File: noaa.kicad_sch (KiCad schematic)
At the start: 12 parts, among them J1 USB_C_Receptacle_USB2.0_16P, J2 SMA_F, J3 SMA_F, U1 MAX2659ELTT, U2 AMS1117-3.3

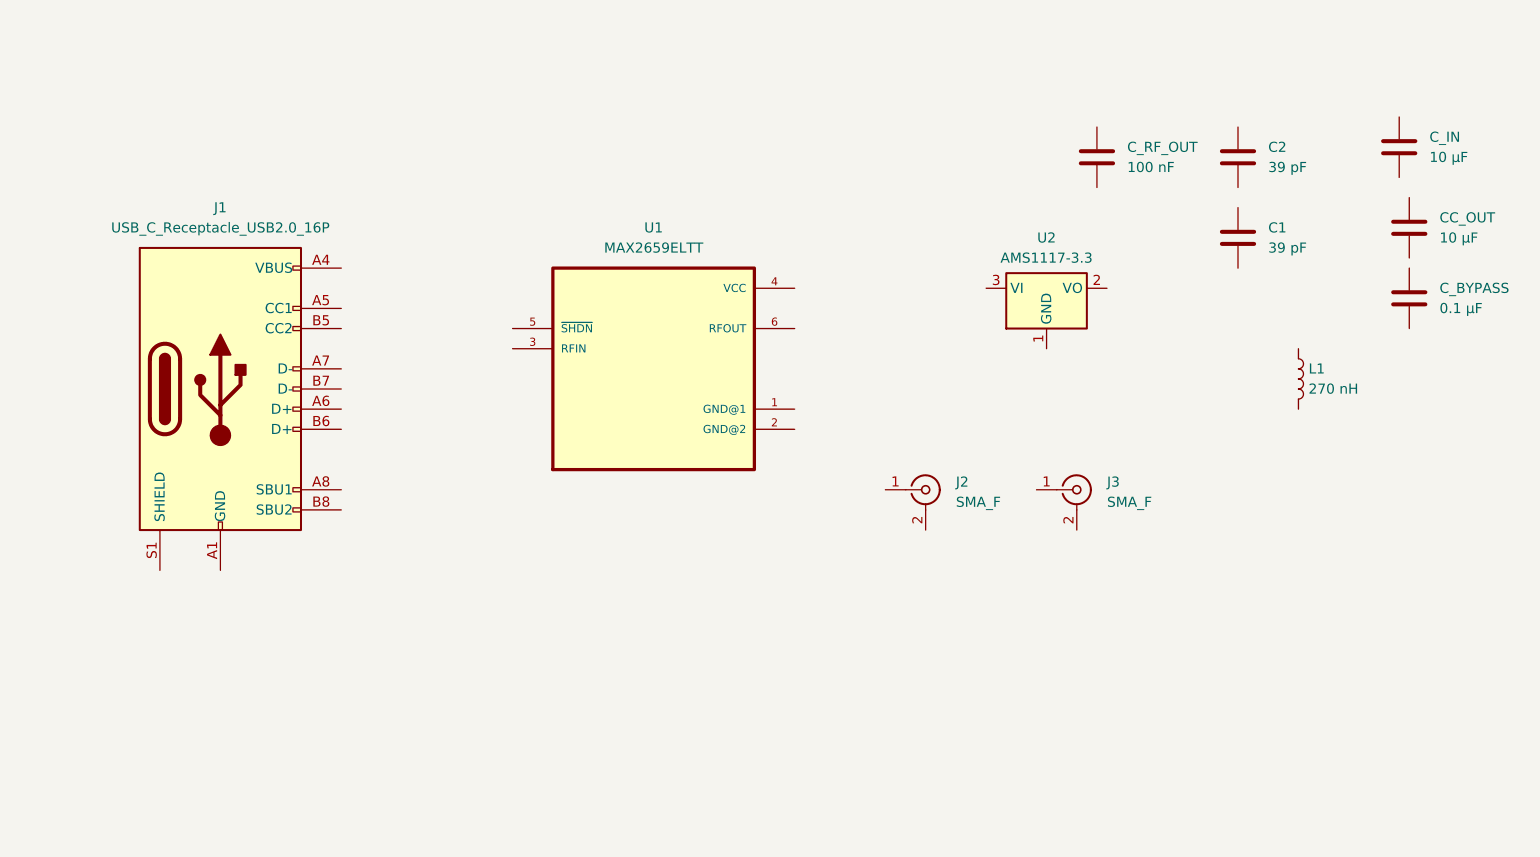
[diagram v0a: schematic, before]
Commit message: Added most of the schematic wiring. Still need to do some USB ground and ESD protections
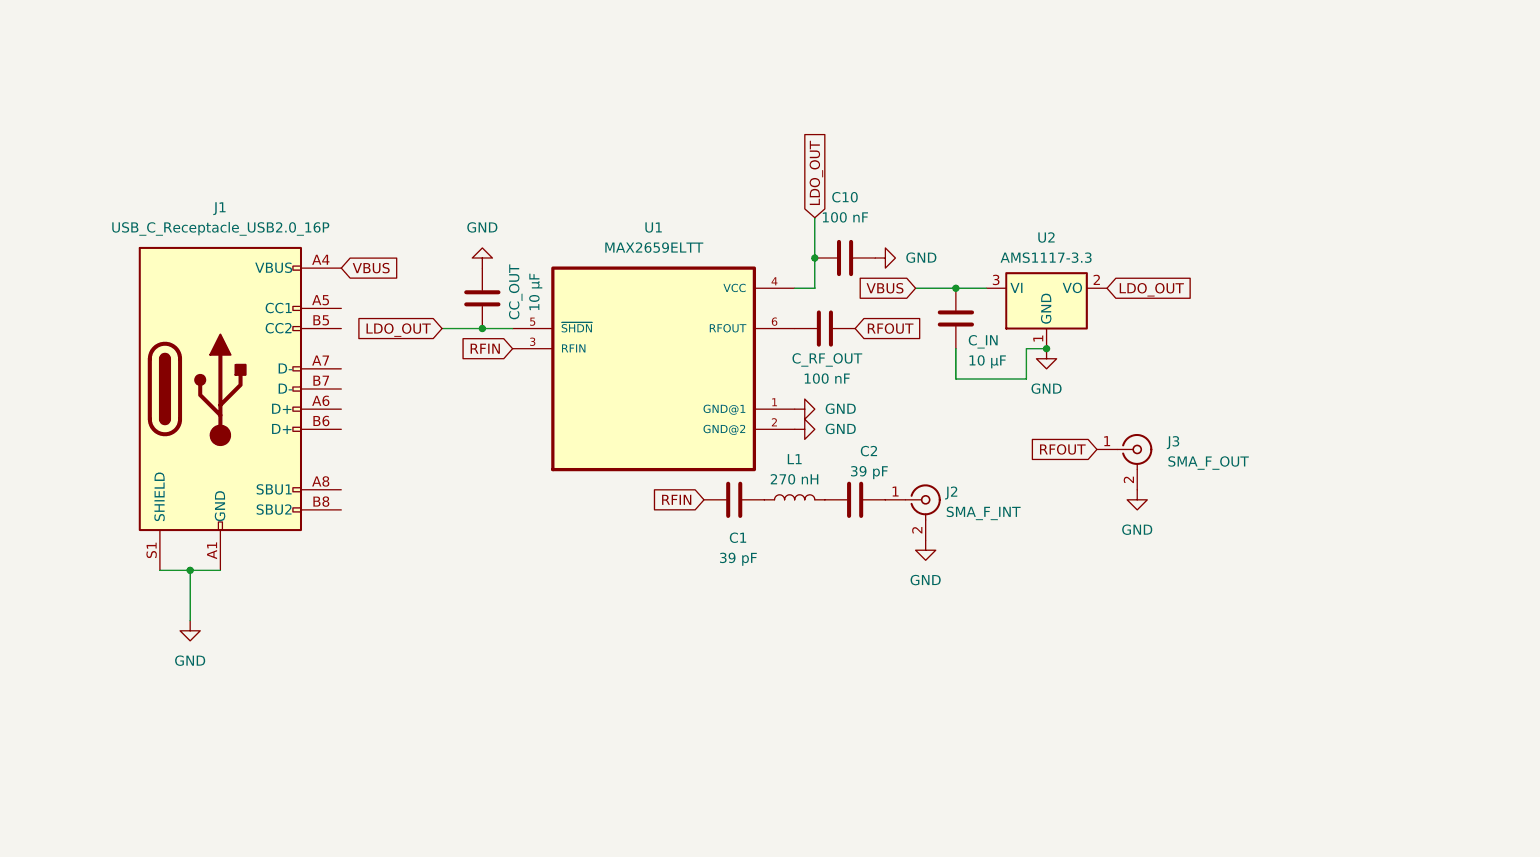
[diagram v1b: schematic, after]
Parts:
- removed C_BYPASS: 0.1 µF, symbol Device:C
- added C10: 100 nF, symbol Device:C
- J2: value SMA_F -> SMA_F_INT
- J3: value SMA_F -> SMA_F_OUT
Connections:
- net at C_RF_OUT.1: now also U1.6 (RFOUT)
- net RFOUT: now reaches C_RF_OUT.2
- net RFOUT: now also J3.1 (In)
- net at J2.1 (In): now also C2.2
- net GND: now reaches J2.2 (Ext)
- net GND: now also CC_OUT.1, C_IN.1, J1.A1 (GND), J1.A12 (GND), J1.B1 (GND), J1.B12 (GND), J1.S1 (SHIELD), J3.2 (Ext), U1.1 (GND@1), U1.2 (GND@2), U2.1 (GND), C10.2
- net LDO_OUT: now reaches CC_OUT.2
- net LDO_OUT: now also U1.4 (VCC), U1.5 (~{SHDN}), U2.2 (VO), C10.1
- net VBUS: now reaches C_IN.2
- net VBUS: now also J1.A4 (VBUS), J1.A9 (VBUS), J1.B4 (VBUS), J1.B9 (VBUS), U2.3 (VI)
- net at L1.1: now also C1.2
- net at L1.2: now also C2.1
- net RFIN: now reaches U1.3 (RFIN)
- net RFIN: now also C1.1
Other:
- moved on the sheet: C1, C2, CC_OUT, C_IN, C_RF_OUT, J2, J3, L1

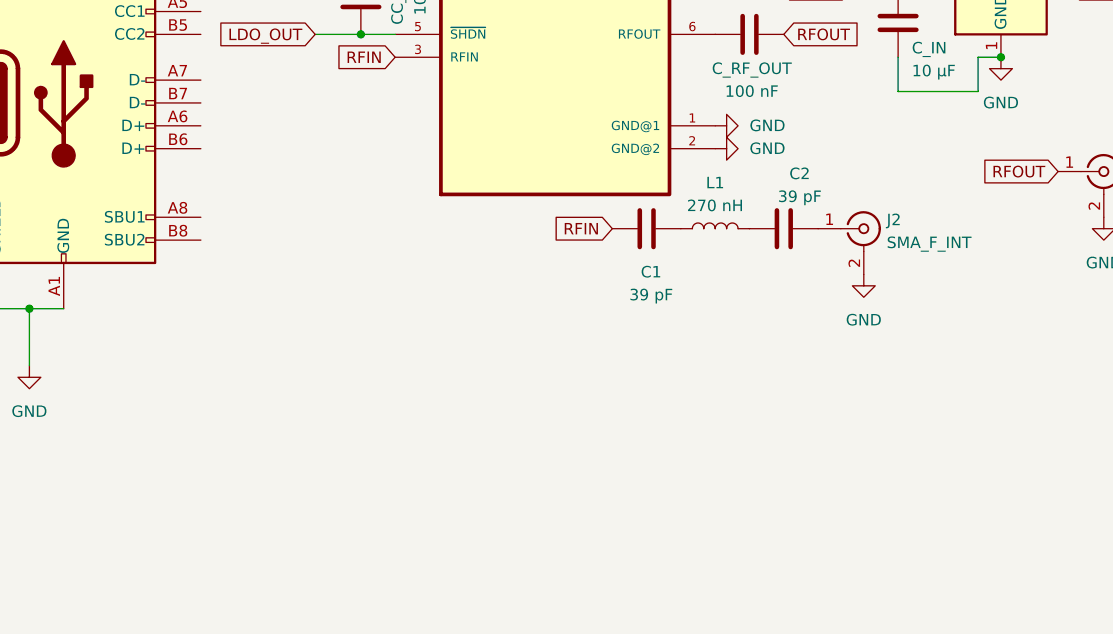
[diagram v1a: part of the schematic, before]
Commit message: Added the ability to switch between freq's for different NOAA's
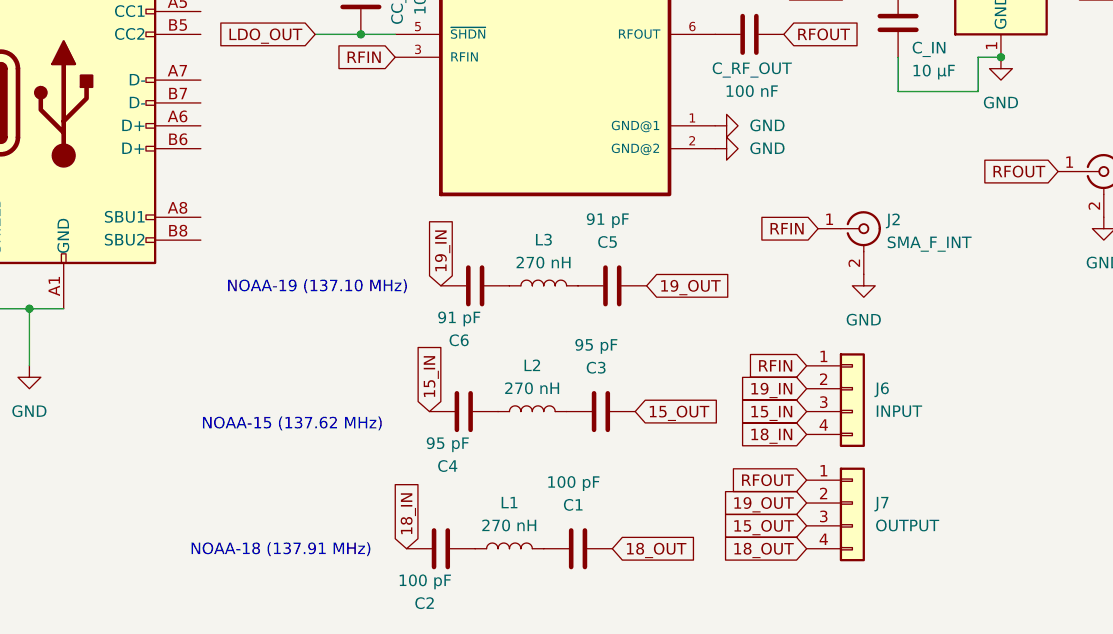
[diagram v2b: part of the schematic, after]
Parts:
- added C3, C4: 95 pF, symbol Device:C
- added C5, C6: 91 pF, symbol Device:C
- added J6: INPUT, Connector_Hirose:Hirose_DF13-04P-1.25DSA_1x04_P1.25mm_Vertical, symbol Connector_Generic:Conn_01x04
- added J7: OUTPUT, Connector_Hirose:Hirose_DF13-04P-1.25DSA_1x04_P1.25mm_Vertical, symbol Connector_Generic:Conn_01x04
- added L2, L3: 270 nH, symbol Device:L
- C1, C2: value 39 pF -> 100 pF
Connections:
- net RFIN: now also J2.1 (In), J6.1 (Pin_1); no longer C1.1
- net RFOUT: now also J7.1 (Pin_1)
- net 18_IN: now reaches C2.2
- net 18_IN: now also J6.4 (Pin_4); no longer J2.1 (In)
- net at L1.1: now also C2.1; no longer C1.2
- net at L1.2: now also C1.2; no longer C2.1
- new net: C6.1, L3.1
- new net: C4.1, L2.1
- new net: C3.2, L2.2
- new net: C5.2, L3.2
- new net 15_IN: C4.2, J6.3 (Pin_3)
- new net 15_OUT: C3.1, J7.3 (Pin_3)
- new net 18_OUT: C1.1, J7.4 (Pin_4)
- new net 19_IN: C6.2, J6.2 (Pin_2)
- new net 19_OUT: C5.1, J7.2 (Pin_2)
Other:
- note added: "NOAA-15 (137.62 MHz)"
- note added: "NOAA-18 (137.91 MHz)"
- note added: "NOAA-19 (137.10 MHz)"
- moved on the sheet: C1, C2, L1

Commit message: Schematic done!
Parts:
- removed C1, C2: 100 pF, symbol Device:C
- removed C3, C4: 95 pF, symbol Device:C
- removed J6: INPUT, Connector_Hirose:Hirose_DF13-04P-1.25DSA_1x04_P1.25mm_Vertical, symbol Connector_Generic:Conn_01x04
- removed J7: OUTPUT, Connector_Hirose:Hirose_DF13-04P-1.25DSA_1x04_P1.25mm_Vertical, symbol Connector_Generic:Conn_01x04
- removed L1, L2: 270 nH, symbol Device:L
- added C7: 1µF, Capacitor_SMD:C_0603_1608Metric, symbol Device:C
- added D1: MBRS340, Diode_SMD:D_SMC, symbol Diode:MBRS340
- added R1, R2: 5.1 kΩ, symbol Device:R
- C5, C6: value 91 pF -> 100 pF
- L3: value 270 nH -> 27 nH
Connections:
- net GND: now also C7.2, R1.2, R2.2; no longer J1.S1 (SHIELD)
- net VBUS: now also D1.2 (A); no longer C_IN.2, U2.3 (VI)
- net at J1.A5 (CC1): now also R1.1
- net at J1.B5 (CC2): now also R2.1
- net 19_IN: no longer names the net of C6.2
- net 19_IN: now also J2.1 (In)
- net 19_OUT: no longer names the net of C5.1
- net 19_OUT: now also U1.3 (RFIN)
- removed net RFIN: J2.1 (In), U1.3 (RFIN)
- new net: C_IN.2, D1.1 (K), U2.3 (VI)
- new net: C7.1, J1.S1 (SHIELD)
- no-connect marks 0 -> 6
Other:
- note removed: "NOAA-15 (137.62 MHz)"
- note removed: "NOAA-18 (137.91 MHz)"
- moved on the sheet: C5, C6, J1, J2, L3

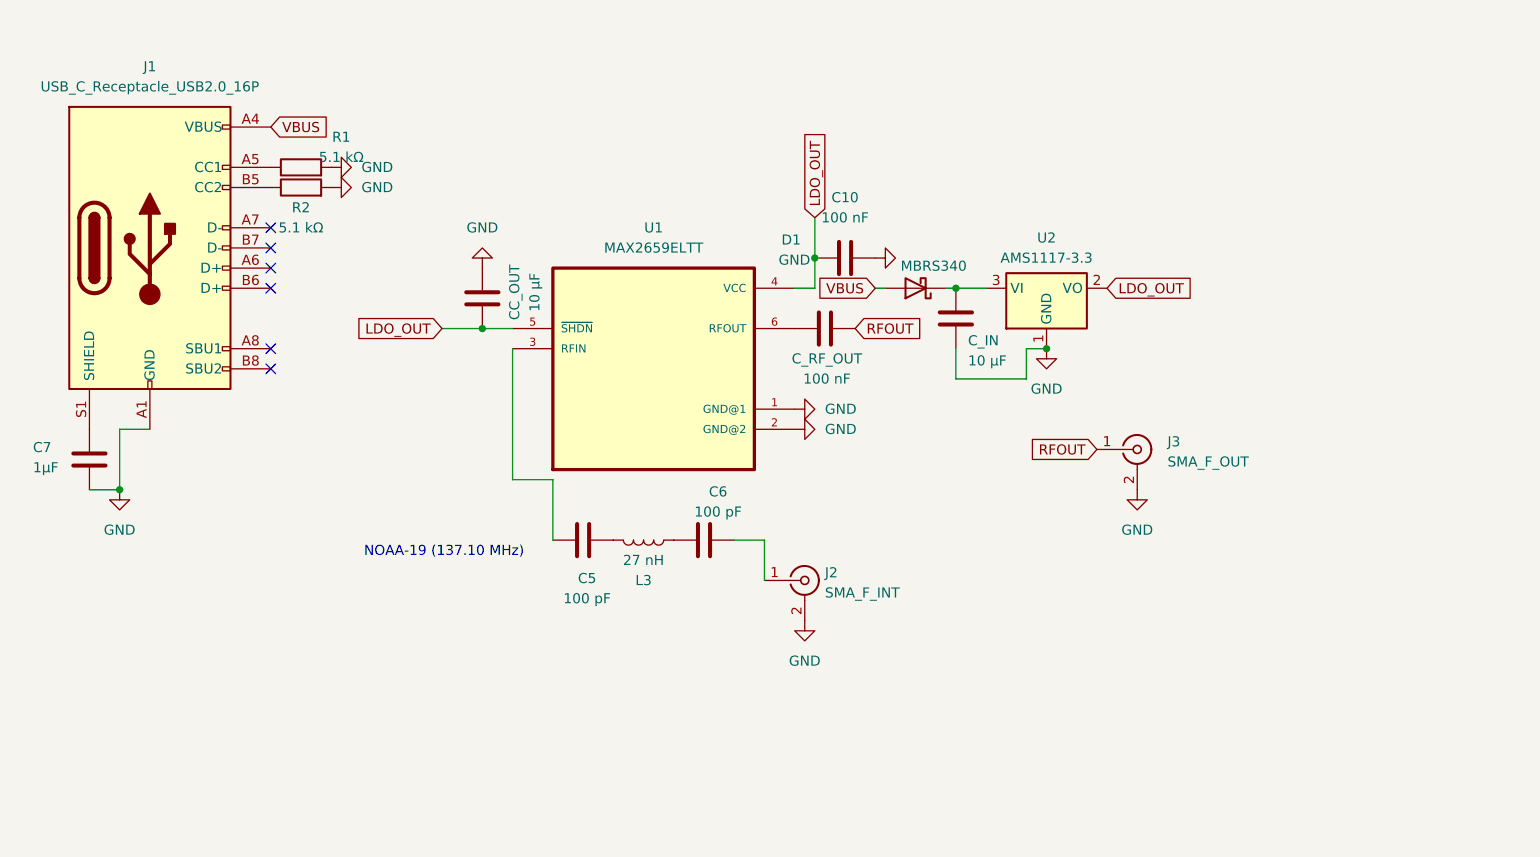
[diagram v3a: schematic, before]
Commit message: Fixed the RF amplified shematic. Time to wire!
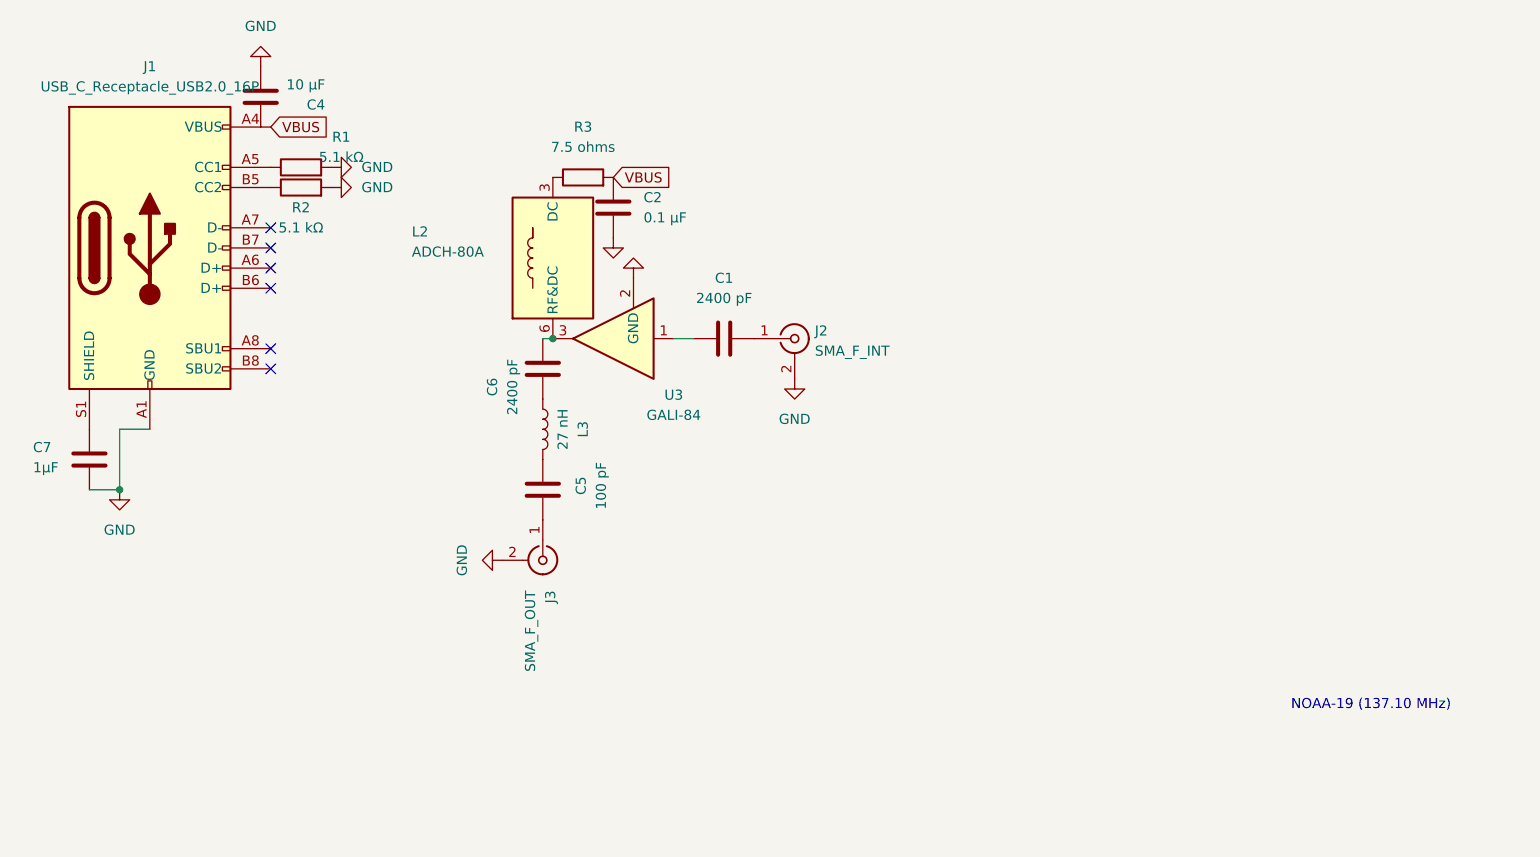
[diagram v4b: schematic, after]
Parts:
- removed C10, C_RF_OUT: 100 nF, symbol Device:C
- removed CC_OUT, C_IN: 10 µF, symbol Device:C
- removed D1: MBRS340, Diode_SMD:D_SMC, symbol Diode:MBRS340
- removed U1: MAX2659ELTT, MAX2659ELTT:SON50P150X100X80-6N, symbol MAX2659ELTT:MAX2659ELTT
- removed U2: AMS1117-3.3, Package_TO_SOT_SMD:SOT-223-3_TabPin2, symbol Regulator_Linear:AMS1117-3.3
- added C1: 2400 pF, symbol Device:C
- added C2: 0.1 μF, symbol Device:C
- added C4: 10 μF, symbol Device:C
- added L2: ADCH-80A, RF_Mini-Circuits:Mini-Circuits_CD542_H2.84mm, symbol RF:ADCH-80A
- added R3: 7.5 ohms, symbol Device:R
- added U3: GALI-84, Package_TO_SOT_SMD:SOT-89-3, symbol RF_Amplifier:GALI-84
- C6: value 100 pF -> 2400 pF
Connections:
- net RFOUT is gone; now on an unnamed net: J3.1 (In)
- net GND: now also C2.1, C4.1, U3.2 (GND)
- net VBUS: now also C2.2, R3.2
- net at C6.2: now also L2.6 (RF&DC), U3.3; no longer J2.1 (In)
- new net: C1.1, U3.1
- new net: C1.2, J2.1 (In)
- new net: L2.3 (DC), R3.1
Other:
- moved on the sheet: C5, C6, J2, J3, L3
